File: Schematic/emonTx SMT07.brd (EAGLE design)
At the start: 100 x 80.3 mm, 115 parts, among them IC1 4066D, IC2 4066D, IC3 LMV324, J1 CON_HEADER_PRG_AVR_ICSP, Q2 DS18B20, U2 ATMEGA32U4, X10 BU-SMA-H, X2 CT2, X3 CT3, X4 STEREOJACK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

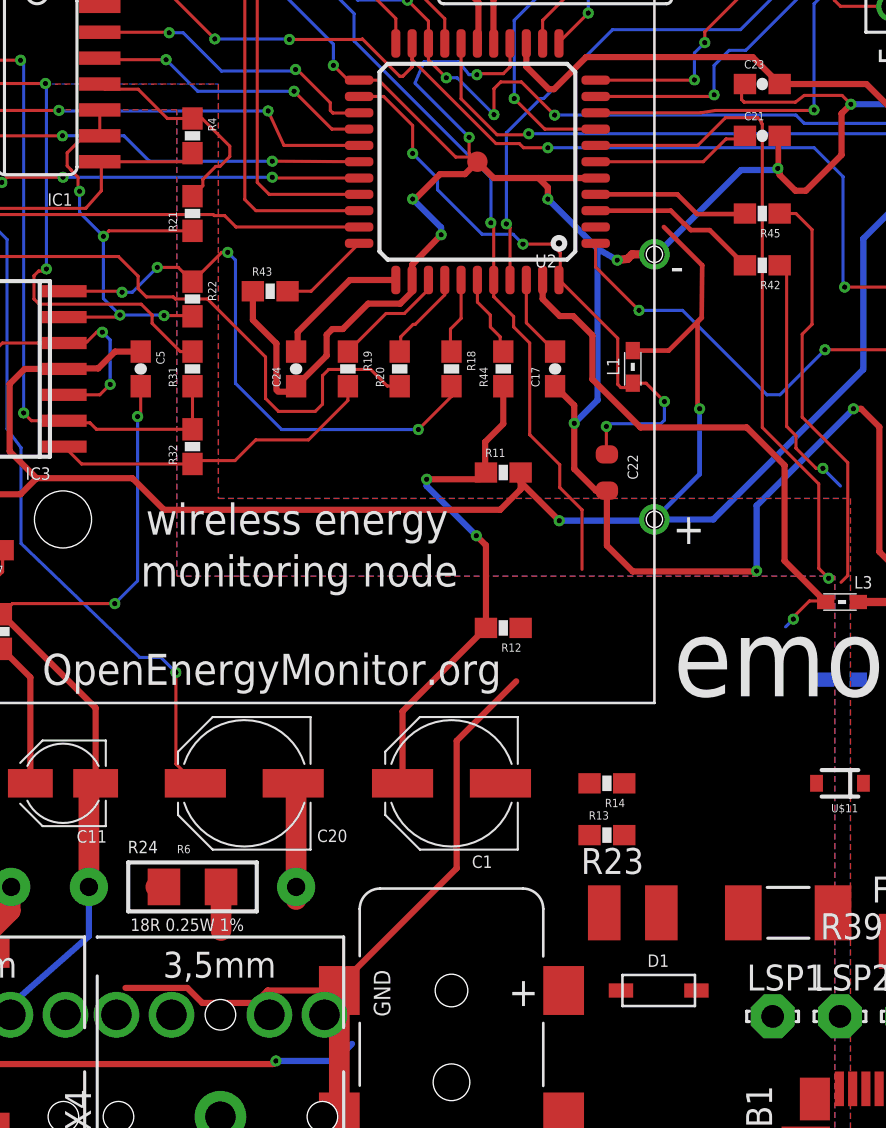
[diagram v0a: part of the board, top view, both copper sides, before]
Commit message: route uvcc to connect to USB 5V
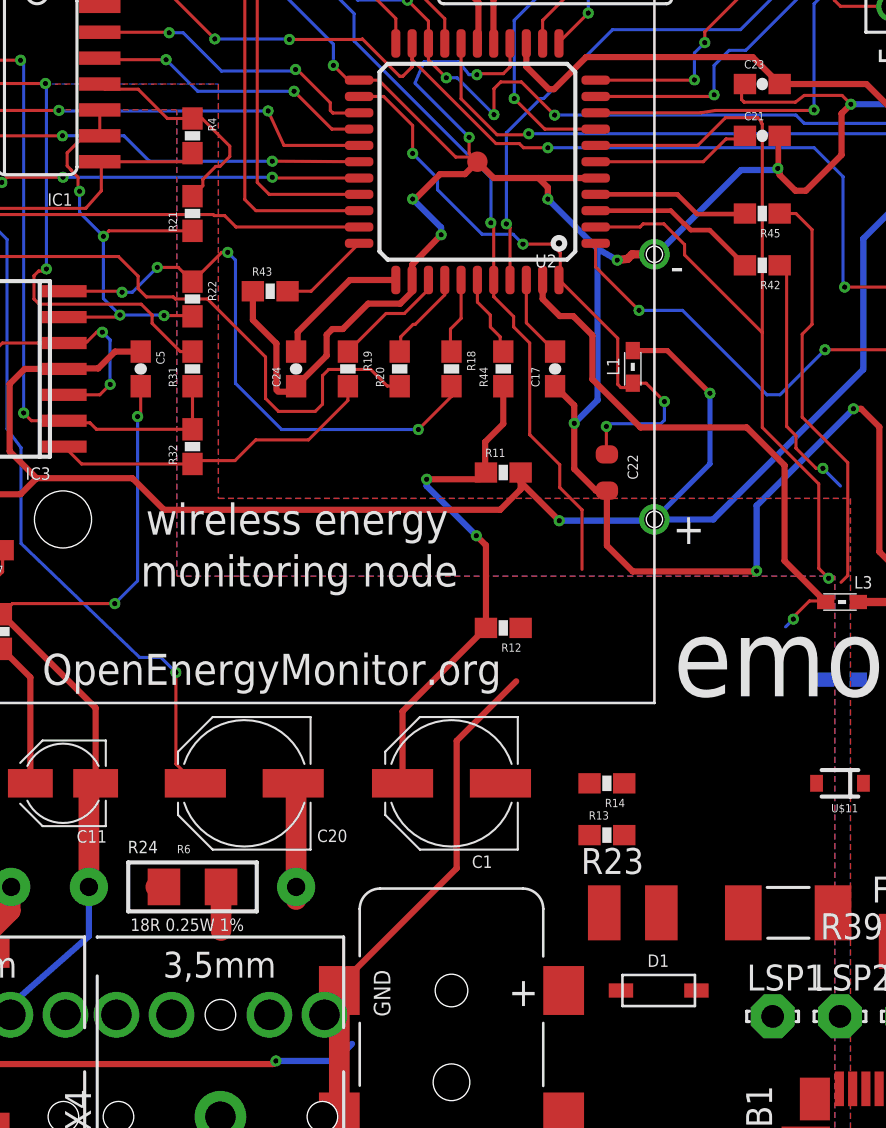
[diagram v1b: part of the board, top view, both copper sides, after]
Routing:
- net AGND: track 237.7 -> 226.6 mm
- net VUSB: track 32.5 -> 43.3 mm
- net 3.3V: track 310.8 -> 302.9 mm
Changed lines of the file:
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@@
 <?xml version="1.0" encoding="utf-8"?>
 <!DOCTYPE eagle SYSTEM "eagle.dtd">
-<eagle version="6.1">
+<eagle version="6.2">
 <drawing>
 <settings>
@@
 <setting verticaltext="up"/>
 </settings>
-<grid distance="50" unitdist="mil" unit="mil" style="lines" multiple="1" display="yes" altdistance="50" altunitdist="mil" altunit="mil"/>
+<grid distance="10" unitdist="mil" unit="mil" style="lines" multiple="1" display="yes" altdistance="50" altunitdist="mil" altunit="mil"/>
 <layers>
 <layer number="1" name="Top" color="4" fill="1" visible="yes" active="yes"/>
@@
 <layer number="16" name="Bottom" color="1" fill="1" visible="yes" active="yes"/>
 <layer number="17" name="Pads" color="2" fill="1" visible="yes" active="yes"/>
-<layer number="18" name="Vias" color="2" fill="1" visible="no" active="yes"/>
+<layer number="18" name="Vias" color="2" fill="1" visible="yes" active="yes"/>
 <layer number="19" name="Unrouted" color="6" fill="1" visible="yes" active="yes"/>
 <layer number="20" name="Dimension" color="15" fill="1" visible="yes" active="yes"/>
@@
 <wire x1="33.02" y1="13.97" x2="33.02" y2="18.72" width="1.016" layer="1"/>
 <wire x1="33.02" y1="18.72" x2="33.35" y2="19.05" width="1.016" layer="1"/>
-<wire x1="45.3" y1="8.89" x2="41.783" y2="8.89" width="0.3048" layer="1"/>
-<wire x1="41.783" y1="8.89" x2="41.1734" y2="8.2804" width="0.3048" layer="1"/>
-<wire x1="41.1734" y1="8.2804" x2="38.5826" y2="8.2804" width="0.3048" layer="1"/>
-<wire x1="38.5826" y1="8.2804" x2="37.846" y2="9.017" width="0.3048" layer="1"/>
-<wire x1="37.846" y1="9.017" x2="34.813" y2="9.017" width="0.3048" layer="1"/>
 <wire x1="45.3" y1="8.89" x2="45.3" y2="9.1304" width="0.3048" layer="1"/>
 <wire x1="45.3" y1="9.1304" x2="51.054" y2="14.8844" width="0.3048" layer="1"/>
@@
 <wire x1="69.0992" y1="27.9908" x2="69.15" y2="27.94" width="0.1524" layer="1"/>
 <contactref element="X4" pad="5"/>
+<wire x1="67.183" y1="26.7208" x2="69.15" y2="24.13" width="0" layer="19" extent="16-16"/>
+<wire x1="68.7" y1="19.05" x2="69.15" y2="24.13" width="0" layer="19" extent="1-16"/>
+<wire x1="59.27" y1="19.05" x2="68.7" y2="19.05" width="0" layer="19" extent="1-1"/>
+<wire x1="53.975" y1="24.0538" x2="59.27" y2="19.05" width="0" layer="19" extent="1-1"/>
+<wire x1="44.57" y1="7.7" x2="45.3" y2="8.89" width="0" layer="19" extent="1-1"/>
+<wire x1="54.19" y1="26.67" x2="53.975" y2="24.0538" width="0" layer="19" extent="1-1"/>
+<wire x1="36.7" y1="13.97" x2="45.3" y2="9.1304" width="0" layer="19" extent="1-1"/>
+<wire x1="33.08" y1="13.91" x2="36.3" y2="13.97" width="0" layer="19" extent="1-1"/>
 </signal>
 <signal name="+5V" class="1">
@@
 <wire x1="57.404" y1="54.6608" x2="65.5692" y2="54.6608" width="0.3048" layer="1"/>
 <wire x1="65.5692" y1="54.6608" x2="66.89" y2="53.34" width="0.3048" layer="1"/>
-<wire x1="61.2136" y1="46.33" x2="63.0936" y2="44.45" width="0.2286" layer="1"/>
-<wire x1="62.865" y1="41.6814" x2="62.865" y2="37.5158" width="0.2286" layer="1"/>
-<wire x1="62.865" y1="37.5158" x2="62.9666" y2="37.4142" width="0.2286" layer="1"/>
-<via x="62.9666" y="37.4142" extent="1-16" drill="0.25"/>
-<wire x1="62.9666" y1="37.4142" x2="62.9666" y2="34.2066" width="0.2286" layer="16"/>
-<wire x1="62.9666" y1="34.2066" x2="60.75" y2="31.99" width="0.2286" layer="16"/>
-<wire x1="59.69" y1="40.27" x2="61.4536" y2="40.27" width="0.2286" layer="1"/>
-<wire x1="61.4536" y1="40.27" x2="62.865" y2="41.6814" width="0.2286" layer="1"/>
+<via x="63.4746" y="38.1762" extent="1-16" drill="0.25"/>
 <wire x1="87.9212" y1="70.4088" x2="87.845" y2="70.485" width="0.3048" layer="1"/>
 <wire x1="92.9" y1="66.42" x2="92.9" y2="67.6534" width="0.3048" layer="1"/>
@@
 <wire x1="56.0832" y1="31.9278" x2="60.6878" y2="31.9278" width="0.3048" layer="16"/>
 <wire x1="60.6878" y1="31.9278" x2="60.75" y2="31.99" width="0.3048" layer="16"/>
-<wire x1="63.0936" y1="44.45" x2="63.0682" y2="41.8846" width="0.2286" layer="1"/>
-<wire x1="63.0682" y1="41.8846" x2="62.865" y2="41.6814" width="0.254" layer="1"/>
 <contactref element="R37" pad="2"/>
 <wire x1="95.416" y1="26.924" x2="92.3544" y2="26.924" width="0.1524" layer="1"/>
 <wire x1="92.3544" y1="26.924" x2="91.8718" y2="27.4066" width="0.1524" layer="1"/>
 <contactref element="U$3" pad="3"/>
+<wire x1="59.69" y1="40.27" x2="61.3808" y2="40.27" width="0.254" layer="1"/>
+<wire x1="61.3808" y1="40.27" x2="63.4746" y2="38.1762" width="0.254" layer="1"/>
+<wire x1="63.4746" y1="38.1762" x2="63.4746" y2="34.7146" width="0.254" layer="16"/>
+<wire x1="63.4746" y1="34.7146" x2="60.75" y2="31.99" width="0.254" layer="16"/>
 <wire x1="92.3544" y1="26.924" x2="93.65" y2="22.86" width="0" layer="19" extent="1-1"/>
 <wire x1="93.98" y1="17.36" x2="93.65" y2="22.86" width="0" layer="19" extent="1-1"/>
@@
 <wire x1="65.9892" y1="51.5112" x2="65.9892" y2="51.435" width="0.1524" layer="1"/>
 <wire x1="65.9892" y1="51.435" x2="66.04" y2="51.3842" width="0.1524" layer="1"/>
-<wire x1="66.04" y1="51.3842" x2="66.04" y2="36.4998" width="0.1524" layer="1"/>
+<wire x1="66.04" y1="51.3842" x2="66.04" y2="41.148" width="0.1524" layer="1"/>
+<wire x1="66.04" y1="41.148" x2="66.04" y2="36.4998" width="0.1524" layer="1"/>
 <wire x1="66.04" y1="36.4998" x2="68.8086" y2="33.7312" width="0.1524" layer="1"/>
 <wire x1="68.8086" y1="33.7312" x2="68.8086" y2="29.591" width="0.1524" layer="1"/>
@@
 <contactref element="LSP1" pad="MP"/>
 <contactref element="U2" pad="2"/>
-<wire x1="57.87" y1="50.33" x2="57.87" y2="46.33" width="0" layer="19" extent="1-1"/>
+<wire x1="57.87" y1="46.33" x2="60.046" y2="46.33" width="0.1524" layer="1"/>
+<wire x1="60.046" y1="46.33" x2="60.198" y2="46.482" width="0.1524" layer="1"/>
+<wire x1="60.198" y1="46.482" x2="61.214" y2="46.482" width="0.1524" layer="1"/>
+<wire x1="61.214" y1="46.482" x2="62.23" y2="45.466" width="0.1524" layer="1"/>
+<wire x1="62.23" y1="45.466" x2="62.23" y2="44.958" width="0.1524" layer="1"/>
+<wire x1="62.23" y1="44.958" x2="66.04" y2="41.148" width="0.1524" layer="1"/>
 <wire x1="72.55" y1="11.3" x2="69.2912" y2="29.1084" width="0" layer="19" extent="1-1"/>
 <wire x1="66.548" y1="7.62" x2="72.55" y2="11.3" width="0" layer="19" extent="1-1"/>

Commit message: update schotkey reverse blocking diode pcb footprint to SOD-123
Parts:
- D1: device adafruit:SOD-123 -> adafruit:SOD-323F
- D2: device adafruit:SOD-323F -> adafruit:SOD-123
- moved F1 2.65 mm to (76.2, 12.7)
- moved U$3 0.76 mm to (90.2, 15.2)
- moved D2 0.06 mm to (81.3, 20.3), turned to 270 degrees
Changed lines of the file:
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@@
 <setting verticaltext="up"/>
 </settings>
-<grid distance="10" unitdist="mil" unit="mil" style="lines" multiple="1" display="yes" altdistance="50" altunitdist="mil" altunit="mil"/>
+<grid distance="50" unitdist="mil" unit="mil" style="lines" multiple="1" display="yes" altdistance="50" altunitdist="mil" altunit="mil"/>
 <layers>
 <layer number="1" name="Top" color="4" fill="1" visible="yes" active="yes"/>
@@
 <attribute name="VALUE" x="17.78" y="10.16" size="1.27" layer="27" rot="R270"/>
 </element>
-<element name="D2" library="adafruit" package="SOD-323F" value="0.5A schottky" x="81.26" y="20.3" smashed="yes" rot="R90">
-<attribute name="NAME" x="80.1568" y="19.8716" size="0.508" layer="25" font="vector" rot="R90"/>
-<attribute name="VALUE" x="82.6298" y="18.7588" size="0.381" layer="27" font="vector" rot="R90"/>
+<element name="D2" library="adafruit" package="SOD-123" value="0.5A schottky" x="81.3" y="20.34" smashed="yes" rot="R270">
+<attribute name="NAME" x="83.6732" y="20.7684" size="0.508" layer="25" font="vector" rot="R270"/>
+<attribute name="VALUE" x="79.9302" y="21.8812" size="0.381" layer="27" font="vector" rot="R270"/>
 </element>
 <element name="3XAAA" library="Battery Holders" package="AAA_PCB_HOLDER" value="4.5V" x="31.75" y="46.99">
@@
 <attribute name="VALUE" x="29.3116" y="34.5948" size="0.6096" layer="27" rot="R180"/>
 </element>
-<element name="F1" library="rcl" package="R1210" value="500mA" x="73.95" y="11.3"/>
+<element name="F1" library="rcl" package="R1210" value="500mA" x="76.2" y="12.7"/>
 <element name="U$6" library="adafruit" package="XBEE" value="XBEE" x="85.09" y="41.91" smashed="yes"/>
-<element name="D1" library="adafruit" package="SOD-123" value="1N4148 30V 150mA (Av)" x="60.96" y="8.89" smashed="yes" rot="R180">
+<element name="D1" library="adafruit" package="SOD-323F" value="1N4148 30V 150mA (Av)" x="60.96" y="8.89" smashed="yes" rot="R180">
 <attribute name="ABBREV" value="emonTx" x="60.96" y="8.89" size="1.778" layer="27" rot="R180" display="off"/>
 <attribute name="DRAWING_AUTHOR" value="Glyn Hudson" x="60.96" y="8.89" size="1.778" layer="27" rot="R180" display="off"/>
@@
 </element>
 <element name="R23" library="rcl" package="R1210" value="40mA Holding 150mA trip" x="59.69" y="12.7"/>
-<element name="U$3" library="OpenEnergyMonitor" package="SOT89" value="MCP1702" x="89.5604" y="15.6972">
-<attribute name="OUTPUT" value="3.3V" x="89.5604" y="15.6972" size="1.778" layer="27" display="off"/>
+<element name="U$3" library="OpenEnergyMonitor" package="SOT89" value="MCP1702" x="90.17" y="15.24">
+<attribute name="OUTPUT" value="3.3V" x="90.17" y="15.24" size="1.778" layer="27" display="off"/>
 </element>
 <element name="H1" library="holes" package="3,0-PAD" value="MOUNT-PAD-ROUND3.0" x="4.2164" y="4.2418"/>
@@
 <contactref element="U$3" pad="2.1"/>
 <wire x1="85.23" y1="22.86" x2="85.23" y2="27.8254" width="0" layer="19" extent="1-1"/>
-<wire x1="81.26" y1="21.3" x2="85.23" y2="22.86" width="0" layer="19" extent="1-1"/>
+<wire x1="81.3" y1="22.19" x2="85.23" y2="22.86" width="0" layer="19" extent="1-1"/>
 <wire x1="85.683" y1="16.8148" x2="85.23" y2="22.86" width="0" layer="19" extent="1-1"/>
-<wire x1="89.5604" y1="16.5862" x2="85.683" y2="16.8148" width="0" layer="19" extent="1-1"/>
-<wire x1="89.5604" y1="13.9702" x2="89.5604" y2="16.5862" width="0" layer="19" extent="1-1"/>
-<wire x1="95.44" y1="12.897" x2="89.5604" y2="13.9702" width="0" layer="19" extent="1-1"/>
-<wire x1="71" y1="19.05" x2="81.26" y2="21.3" width="0" layer="19" extent="1-1"/>
+<wire x1="90.17" y1="16.129" x2="85.683" y2="16.8148" width="0" layer="19" extent="1-1"/>
+<wire x1="90.17" y1="13.513" x2="90.17" y2="16.129" width="0" layer="19" extent="1-1"/>
+<wire x1="95.44" y1="12.897" x2="90.17" y2="13.513" width="0" layer="19" extent="1-1"/>
+<wire x1="71" y1="19.05" x2="81.3" y2="22.19" width="0" layer="19" extent="1-1"/>
 <wire x1="45.9232" y1="6.2738" x2="71" y2="19.05" width="0" layer="19" extent="1-16"/>
 </signal>
@@
 <contactref element="F1" pad="2"/>
 <contactref element="D2" pad="A"/>
-<wire x1="75.35" y1="11.3" x2="81.26" y2="19.3" width="0" layer="19" extent="1-1"/>
+<wire x1="77.6" y1="12.7" x2="81.3" y2="18.49" width="0" layer="19" extent="1-1"/>
 </signal>
 <signal name="N$9">
@@
 <wire x1="92.3544" y1="26.924" x2="93.65" y2="22.86" width="0" layer="19" extent="1-1"/>
 <wire x1="93.98" y1="17.36" x2="93.65" y2="22.86" width="0" layer="19" extent="1-1"/>
-<wire x1="91.0594" y1="13.7162" x2="93.98" y2="17.36" width="0" layer="19" extent="1-1"/>
+<wire x1="91.669" y1="13.259" x2="93.98" y2="17.36" width="0" layer="19" extent="1-1"/>
 <wire x1="43.18" y1="40.22" x2="35.56" y2="40.22" width="0" layer="19" extent="1-1"/>
 </signal>
@@
 <contactref element="D1" pad="C"/>
 <contactref element="R39" pad="1"/>
-<wire x1="62.81" y1="8.89" x2="65.11" y2="12.7" width="0" layer="19" extent="1-1"/>
+<wire x1="59.96" y1="8.89" x2="65.11" y2="12.7" width="0" layer="19" extent="1-1"/>
 </signal>
 <signal name="N$17">
@@
 <wire x1="62.23" y1="45.466" x2="62.23" y2="44.958" width="0.1524" layer="1"/>
 <wire x1="62.23" y1="44.958" x2="66.04" y2="41.148" width="0.1524" layer="1"/>
-<wire x1="72.55" y1="11.3" x2="69.2912" y2="29.1084" width="0" layer="19" extent="1-1"/>
-<wire x1="66.548" y1="7.62" x2="72.55" y2="11.3" width="0" layer="19" extent="1-1"/>
+<wire x1="74.8" y1="12.7" x2="69.2912" y2="29.1084" width="0" layer="19" extent="1-1"/>
+<wire x1="66.548" y1="7.62" x2="74.8" y2="12.7" width="0" layer="19" extent="1-1"/>
 <wire x1="69.82" y1="4.07" x2="66.548" y2="7.62" width="0" layer="19" extent="1-1"/>
 </signal>
@@
 <contactref element="D1" pad="A"/>
 <contactref element="R23" pad="2"/>
-<wire x1="59.11" y1="8.89" x2="61.09" y2="12.7" width="0" layer="19" extent="1-1"/>
+<wire x1="61.96" y1="8.89" x2="61.09" y2="12.7" width="0" layer="19" extent="1-1"/>
 </signal>
 </signals>
